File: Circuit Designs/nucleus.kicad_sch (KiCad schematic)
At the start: 73 parts

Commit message: deleted previous version files
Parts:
- removed R? (x2): 22R, CoF_Resistor:R-0402, symbol CoE_Resistor:22R
- C34, C35, C36, C37, C38, C39, C40, C41, C42, C43, C44, C45, C46, C47, C48, C49, C50, C51, C52, C53, C54, C55: renamed from C?; footprint Capacitor_SMD:C_0402_1005Metric -> CoF_Capacitor:C-0402
- gave numbers to parts that had none: 49
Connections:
- net USBD+: now also U2.45 (PA12)
- net USBD-: now also U2.44 (PA11)

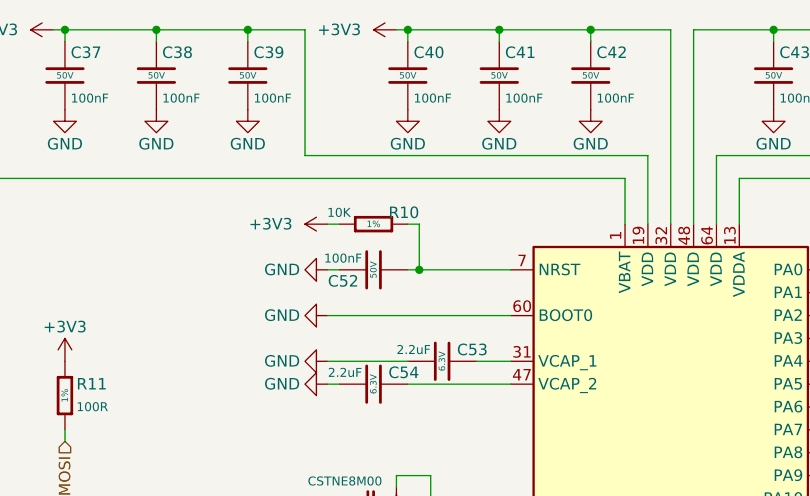
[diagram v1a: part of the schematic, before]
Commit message: changed the LED packages, edited field reference positions
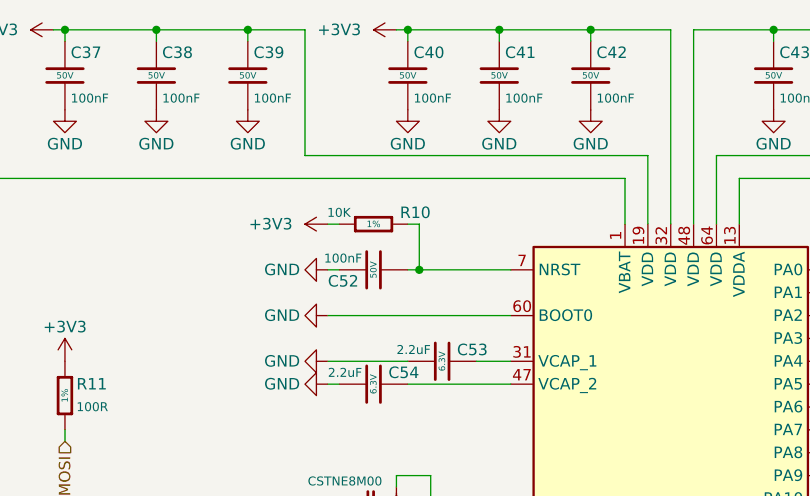
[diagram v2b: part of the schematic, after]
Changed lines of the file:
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@@
   (symbol (lib_id "CoE_Resistor:10K") (at 118.11 38.1 90) (unit 1)
     (in_bom yes) (on_board yes)
-    (property "Reference" "R10" (id 0) (at 123.19 36.83 90)
+    (property "Reference" "R10" (id 0) (at 124.46 36.83 90)
       (effects (font (size 1.27 1.27)) (justify left))
     )
@@
       (effects (font (size 1.27 1.27)) (justify bottom) hide)
     )
-    (property "Datasheet" "https://datasheet.lcsc.com/lcsc/1810231112_Hubei-KENTO-Elec-KT-0603R_C2286.pdf" (id 3) (at 233.172 147.574 0)
+    (property "Datasheet" "https://datasheet.lcsc.com/lcsc/1810231112_Hubei-KENTO-Elec-KT-0603R_C2286.pdf" (id 3) (at 219.71 162.56 0)
       (effects (font (size 1.27 1.27)) hide)
     )
@@
       (effects (font (size 1.27 1.27)) (justify bottom) hide)
     )
-    (property "Datasheet" "https://datasheet.lcsc.com/lcsc/1810011020_BrtLed-Bright-LED-Elec-BL-HJC36A-AV-TRB_C138546.pdf" (id 3) (at 68.072 147.574 0)
+    (property "Datasheet" "https://datasheet.lcsc.com/lcsc/1810011020_BrtLed-Bright-LED-Elec-BL-HJC36A-AV-TRB_C138546.pdf" (id 3) (at 54.61 162.56 0)
       (effects (font (size 1.27 1.27)) hide)
     )
@@
       (effects (font (size 1.27 1.27)) (justify bottom) hide)
     )
-    (property "Datasheet" "https://datasheet.lcsc.com/lcsc/1810231112_Hubei-KENTO-Elec-KT-0603R_C2286.pdf" (id 3) (at 80.772 147.574 0)
+    (property "Datasheet" "https://datasheet.lcsc.com/lcsc/1810231112_Hubei-KENTO-Elec-KT-0603R_C2286.pdf" (id 3) (at 67.31 162.56 0)
       (effects (font (size 1.27 1.27)) hide)
     )
@@
       (effects (font (size 1.27 1.27)) (justify bottom) hide)
     )
-    (property "Datasheet" "https://datasheet.lcsc.com/lcsc/1810011020_BrtLed-Bright-LED-Elec-BL-HJC36A-AV-TRB_C138546.pdf" (id 3) (at 93.472 147.574 0)
+    (property "Datasheet" "https://datasheet.lcsc.com/lcsc/1810011020_BrtLed-Bright-LED-Elec-BL-HJC36A-AV-TRB_C138546.pdf" (id 3) (at 80.01 162.56 0)
       (effects (font (size 1.27 1.27)) hide)
     )
@@
       (effects (font (size 1.27 1.27)) (justify bottom) hide)
     )
-    (property "Datasheet" "https://datasheet.lcsc.com/lcsc/1810231112_Hubei-KENTO-Elec-KT-0603R_C2286.pdf" (id 3) (at 106.172 147.574 0)
+    (property "Datasheet" "https://datasheet.lcsc.com/lcsc/1810231112_Hubei-KENTO-Elec-KT-0603R_C2286.pdf" (id 3) (at 92.71 162.56 0)
       (effects (font (size 1.27 1.27)) hide)
     )
@@
       (effects (font (size 1.27 1.27)) (justify bottom) hide)
     )
-    (property "Datasheet" "https://datasheet.lcsc.com/lcsc/1810011020_BrtLed-Bright-LED-Elec-BL-HJC36A-AV-TRB_C138546.pdf" (id 3) (at 118.872 147.574 0)
+    (property "Datasheet" "https://datasheet.lcsc.com/lcsc/1810011020_BrtLed-Bright-LED-Elec-BL-HJC36A-AV-TRB_C138546.pdf" (id 3) (at 105.41 162.56 0)
       (effects (font (size 1.27 1.27)) hide)
     )
@@
       (effects (font (size 1.27 1.27)) (justify bottom) hide)
     )
-    (property "Datasheet" "https://datasheet.lcsc.com/lcsc/1810231112_Hubei-KENTO-Elec-KT-0603R_C2286.pdf" (id 3) (at 131.572 147.574 0)
+    (property "Datasheet" "https://datasheet.lcsc.com/lcsc/1810231112_Hubei-KENTO-Elec-KT-0603R_C2286.pdf" (id 3) (at 118.11 162.56 0)
       (effects (font (size 1.27 1.27)) hide)
     )
@@
       (effects (font (size 1.27 1.27)) (justify bottom) hide)
     )
-    (property "Datasheet" "https://datasheet.lcsc.com/lcsc/1810011020_BrtLed-Bright-LED-Elec-BL-HJC36A-AV-TRB_C138546.pdf" (id 3) (at 144.272 147.574 0)
+    (property "Datasheet" "https://datasheet.lcsc.com/lcsc/1810011020_BrtLed-Bright-LED-Elec-BL-HJC36A-AV-TRB_C138546.pdf" (id 3) (at 130.81 162.56 0)
       (effects (font (size 1.27 1.27)) hide)
     )
@@
       (effects (font (size 1.27 1.27)) (justify bottom) hide)
     )
-    (property "Datasheet" "https://datasheet.lcsc.com/lcsc/1810231112_Hubei-KENTO-Elec-KT-0603R_C2286.pdf" (id 3) (at 156.972 147.574 0)
+    (property "Datasheet" "https://datasheet.lcsc.com/lcsc/1810231112_Hubei-KENTO-Elec-KT-0603R_C2286.pdf" (id 3) (at 143.51 162.56 0)
       (effects (font (size 1.27 1.27)) hide)
     )
@@
       (effects (font (size 1.27 1.27)) (justify bottom) hide)
     )
-    (property "Datasheet" "https://datasheet.lcsc.com/lcsc/1810011020_BrtLed-Bright-LED-Elec-BL-HJC36A-AV-TRB_C138546.pdf" (id 3) (at 169.672 147.574 0)
+    (property "Datasheet" "https://datasheet.lcsc.com/lcsc/1810011020_BrtLed-Bright-LED-Elec-BL-HJC36A-AV-TRB_C138546.pdf" (id 3) (at 156.21 162.56 0)
       (effects (font (size 1.27 1.27)) hide)
     )
@@
       (effects (font (size 1.27 1.27)) (justify bottom) hide)
     )
-    (property "Datasheet" "https://datasheet.lcsc.com/lcsc/1810231112_Hubei-KENTO-Elec-KT-0603R_C2286.pdf" (id 3) (at 182.372 147.574 0)
+    (property "Datasheet" "https://datasheet.lcsc.com/lcsc/1810231112_Hubei-KENTO-Elec-KT-0603R_C2286.pdf" (id 3) (at 168.91 162.56 0)
       (effects (font (size 1.27 1.27)) hide)
     )
@@
       (effects (font (size 1.27 1.27)) (justify bottom) hide)
     )
-    (property "Datasheet" "https://datasheet.lcsc.com/lcsc/1810011020_BrtLed-Bright-LED-Elec-BL-HJC36A-AV-TRB_C138546.pdf" (id 3) (at 195.072 147.574 0)
+    (property "Datasheet" "https://datasheet.lcsc.com/lcsc/1810011020_BrtLed-Bright-LED-Elec-BL-HJC36A-AV-TRB_C138546.pdf" (id 3) (at 181.61 162.56 0)
       (effects (font (size 1.27 1.27)) hide)
     )
@@
       (effects (font (size 1.27 1.27)) (justify bottom) hide)
     )
-    (property "Datasheet" "https://datasheet.lcsc.com/lcsc/1810231112_Hubei-KENTO-Elec-KT-0603R_C2286.pdf" (id 3) (at 207.772 147.574 0)
+    (property "Datasheet" "https://datasheet.lcsc.com/lcsc/1810231112_Hubei-KENTO-Elec-KT-0603R_C2286.pdf" (id 3) (at 194.31 162.56 0)
       (effects (font (size 1.27 1.27)) hide)
     )
@@
       (effects (font (size 1.27 1.27)) (justify bottom) hide)
     )
-    (property "Datasheet" "https://datasheet.lcsc.com/lcsc/1810011020_BrtLed-Bright-LED-Elec-BL-HJC36A-AV-TRB_C138546.pdf" (id 3) (at 220.472 147.574 0)
+    (property "Datasheet" "https://datasheet.lcsc.com/lcsc/1810011020_BrtLed-Bright-LED-Elec-BL-HJC36A-AV-TRB_C138546.pdf" (id 3) (at 207.01 162.56 0)
       (effects (font (size 1.27 1.27)) hide)
     )
@@
       (effects (font (size 1.27 1.27)) (justify bottom) hide)
     )
-    (property "Datasheet" "https://datasheet.lcsc.com/lcsc/1810011020_BrtLed-Bright-LED-Elec-BL-HJC36A-AV-TRB_C138546.pdf" (id 3) (at 245.872 147.574 0)
+    (property "Datasheet" "https://datasheet.lcsc.com/lcsc/1810011020_BrtLed-Bright-LED-Elec-BL-HJC36A-AV-TRB_C138546.pdf" (id 3) (at 232.41 162.56 0)
       (effects (font (size 1.27 1.27)) hide)
     )
@@
       (effects (font (size 1.27 1.27)) (justify bottom) hide)
     )
-    (property "Datasheet" "https://datasheet.lcsc.com/lcsc/1810231112_Hubei-KENTO-Elec-KT-0603R_C2286.pdf" (id 3) (at 258.572 147.574 0)
+    (property "Datasheet" "https://datasheet.lcsc.com/lcsc/1810231112_Hubei-KENTO-Elec-KT-0603R_C2286.pdf" (id 3) (at 245.11 162.56 0)
       (effects (font (size 1.27 1.27)) hide)
     )
@@
       (effects (font (size 1.27 1.27)) (justify bottom) hide)
     )
-    (property "Datasheet" "https://datasheet.lcsc.com/lcsc/1810011020_BrtLed-Bright-LED-Elec-BL-HJC36A-AV-TRB_C138546.pdf" (id 3) (at 271.272 147.574 0)
-      (effects (font (size 1.27 1.27)) hide)
-    )
+    (property "Datasheet" "https://datasheet.lcsc.com/lcsc/1810011020_BrtLed-Bright-LED-Elec-BL-HJC36A-AV-TRB_C138546.pdf" (id 3) (at 257.81 162.56 0)
+      (effects (font (size 1.27 1.27)) hide)
+    )

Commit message: edited the motor driver's and the current amplifier's packages
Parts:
- D1, D10, D11, D12, D13, D14, D15, D16, D17, D2, D3, D4, D5, D6, D7, D8, D9: footprint LED_SMD:LED_0603_1608Metric -> CoF_Diode:LED-0603
- Q1, Q2: footprint Package_TO_SOT_SMD:TSOT-23 -> CoF_SmallOutline:SOT-23
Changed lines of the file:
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@@
       (effects (font (size 0.9906 0.9906)) (justify left))
     )
-    (property "Footprint" "Package_TO_SOT_SMD:TSOT-23" (id 2) (at 99.06 154.94 0)
+    (property "Footprint" "CoF_SmallOutline:SOT-23" (id 2) (at 99.06 154.94 0)
       (effects (font (size 1.27 1.27)) (justify bottom) hide)
     )
@@
       (effects (font (size 0.9906 0.9906)) (justify left))
     )
-    (property "Footprint" "Package_TO_SOT_SMD:TSOT-23" (id 2) (at 74.93 154.94 0)
+    (property "Footprint" "CoF_SmallOutline:SOT-23" (id 2) (at 74.93 154.94 0)
       (effects (font (size 1.27 1.27)) (justify bottom) hide)
     )
@@
       (effects (font (size 0.9906 0.9906)) (justify left))
     )
-    (property "Footprint" "LED_SMD:LED_0603_1608Metric" (id 2) (at 219.71 135.89 0)
+    (property "Footprint" "CoF_Diode:LED-0603" (id 2) (at 219.71 135.89 0)
       (effects (font (size 1.27 1.27)) (justify bottom) hide)
     )
@@
       (effects (font (size 0.9906 0.9906)) (justify left))
     )
-    (property "Footprint" "LED_SMD:LED_0603_1608Metric" (id 2) (at 54.61 135.89 0)
+    (property "Footprint" "CoF_Diode:LED-0603" (id 2) (at 54.61 135.89 0)
       (effects (font (size 1.27 1.27)) (justify bottom) hide)
     )
@@
       (effects (font (size 0.9906 0.9906)) (justify left))
     )
-    (property "Footprint" "LED_SMD:LED_0603_1608Metric" (id 2) (at 67.31 135.89 0)
+    (property "Footprint" "CoF_Diode:LED-0603" (id 2) (at 67.31 135.89 0)
       (effects (font (size 1.27 1.27)) (justify bottom) hide)
     )
@@
       (effects (font (size 0.9906 0.9906)) (justify left))
     )
-    (property "Footprint" "LED_SMD:LED_0603_1608Metric" (id 2) (at 80.01 135.89 0)
+    (property "Footprint" "CoF_Diode:LED-0603" (id 2) (at 80.01 135.89 0)
       (effects (font (size 1.27 1.27)) (justify bottom) hide)
     )
@@
       (effects (font (size 0.9906 0.9906)) (justify left))
     )
-    (property "Footprint" "LED_SMD:LED_0603_1608Metric" (id 2) (at 92.71 135.89 0)
+    (property "Footprint" "CoF_Diode:LED-0603" (id 2) (at 92.71 135.89 0)
       (effects (font (size 1.27 1.27)) (justify bottom) hide)
     )
@@
       (effects (font (size 0.9906 0.9906)) (justify left))
     )
-    (property "Footprint" "LED_SMD:LED_0603_1608Metric" (id 2) (at 105.41 135.89 0)
+    (property "Footprint" "CoF_Diode:LED-0603" (id 2) (at 105.41 135.89 0)
       (effects (font (size 1.27 1.27)) (justify bottom) hide)
     )
@@
       (effects (font (size 0.9906 0.9906)) (justify left))
     )
-    (property "Footprint" "LED_SMD:LED_0603_1608Metric" (id 2) (at 118.11 135.89 0)
+    (property "Footprint" "CoF_Diode:LED-0603" (id 2) (at 118.11 135.89 0)
       (effects (font (size 1.27 1.27)) (justify bottom) hide)
     )
@@
       (effects (font (size 0.9906 0.9906)) (justify left))
     )
-    (property "Footprint" "LED_SMD:LED_0603_1608Metric" (id 2) (at 130.81 135.89 0)
+    (property "Footprint" "CoF_Diode:LED-0603" (id 2) (at 130.81 135.89 0)
       (effects (font (size 1.27 1.27)) (justify bottom) hide)
     )
@@
       (effects (font (size 0.9906 0.9906)) (justify left))
     )
-    (property "Footprint" "LED_SMD:LED_0603_1608Metric" (id 2) (at 143.51 135.89 0)
+    (property "Footprint" "CoF_Diode:LED-0603" (id 2) (at 143.51 135.89 0)
       (effects (font (size 1.27 1.27)) (justify bottom) hide)
     )
@@
       (effects (font (size 0.9906 0.9906)) (justify left))
     )
-    (property "Footprint" "LED_SMD:LED_0603_1608Metric" (id 2) (at 156.21 135.89 0)
+    (property "Footprint" "CoF_Diode:LED-0603" (id 2) (at 156.21 135.89 0)
       (effects (font (size 1.27 1.27)) (justify bottom) hide)
     )
@@
       (effects (font (size 0.9906 0.9906)) (justify left))
     )
-    (property "Footprint" "LED_SMD:LED_0603_1608Metric" (id 2) (at 168.91 135.89 0)
+    (property "Footprint" "CoF_Diode:LED-0603" (id 2) (at 168.91 135.89 0)
       (effects (font (size 1.27 1.27)) (justify bottom) hide)
     )
@@
       (effects (font (size 0.9906 0.9906)) (justify left))
     )
-    (property "Footprint" "LED_SMD:LED_0603_1608Metric" (id 2) (at 181.61 135.89 0)
+    (property "Footprint" "CoF_Diode:LED-0603" (id 2) (at 181.61 135.89 0)
       (effects (font (size 1.27 1.27)) (justify bottom) hide)
     )
@@
       (effects (font (size 0.9906 0.9906)) (justify left))
     )
-    (property "Footprint" "LED_SMD:LED_0603_1608Metric" (id 2) (at 194.31 135.89 0)
+    (property "Footprint" "CoF_Diode:LED-0603" (id 2) (at 194.31 135.89 0)
       (effects (font (size 1.27 1.27)) (justify bottom) hide)
     )
@@
       (effects (font (size 0.9906 0.9906)) (justify left))
     )
-    (property "Footprint" "LED_SMD:LED_0603_1608Metric" (id 2) (at 207.01 135.89 0)
+    (property "Footprint" "CoF_Diode:LED-0603" (id 2) (at 207.01 135.89 0)
       (effects (font (size 1.27 1.27)) (justify bottom) hide)
     )
@@
       (effects (font (size 0.9906 0.9906)) (justify left))
     )
-    (property "Footprint" "LED_SMD:LED_0603_1608Metric" (id 2) (at 232.41 135.89 0)
+    (property "Footprint" "CoF_Diode:LED-0603" (id 2) (at 232.41 135.89 0)
       (effects (font (size 1.27 1.27)) (justify bottom) hide)
     )
@@
       (effects (font (size 0.9906 0.9906)) (justify left))
     )
-    (property "Footprint" "LED_SMD:LED_0603_1608Metric" (id 2) (at 245.11 135.89 0)
+    (property "Footprint" "CoF_Diode:LED-0603" (id 2) (at 245.11 135.89 0)
       (effects (font (size 1.27 1.27)) (justify bottom) hide)
     )
@@
       (effects (font (size 0.9906 0.9906)) (justify left))
     )
-    (property "Footprint" "LED_SMD:LED_0603_1608Metric" (id 2) (at 257.81 135.89 0)
-      (effects (font (size 1.27 1.27)) (justify bottom) hide)
-    )
+    (property "Footprint" "CoF_Diode:LED-0603" (id 2) (at 257.81 135.89 0)
+      (effects (font (size 1.27 1.27)) (justify bottom) hide)
+    )

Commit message: done all the packages and migrations. Now, time to start to route the module
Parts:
- J5: footprint (none) -> CoF_Connector:SoicBite
- U2: footprint Package_QFP:LQFP-64_10x10mm_P0.5mm -> CoF_QuadFlat:LQFP-64
- Y1: footprint (none) -> CoF_Crystal:CSTNE

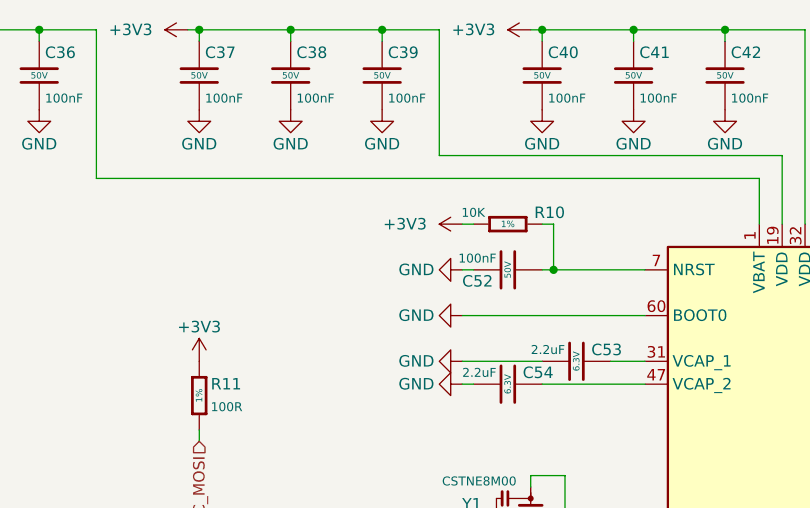
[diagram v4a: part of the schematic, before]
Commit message: done the connection between the MCU and the motor driver
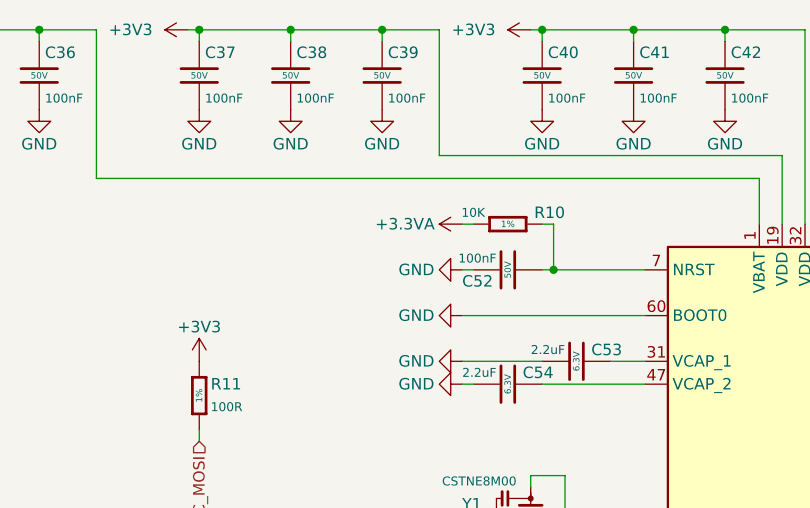
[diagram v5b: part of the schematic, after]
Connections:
- net +3.3VA: now also R10.1
- net +3V3: no longer R10.1
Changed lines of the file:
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@@
-    (pin "1")
-  )
-  (symbol (lib_id "power:+3V3") (at 113.03 38.1 90) (unit 1)
-    (in_bom yes) (on_board yes)
-    (property "Reference" "#PWR060" (id 0) (at 116.84 38.1 0)
-      (effects (font (size 1.27 1.27)) hide)
-    )
-    (property "Value" "+3V3" (id 1) (at 106.68 38.1 90))
-    (property "Footprint" "" (id 2) (at 113.03 38.1 0)
-      (effects (font (size 1.27 1.27)) hide)
-    )
-    (property "Datasheet" "" (id 3) (at 113.03 38.1 0)
-      (effects (font (size 1.27 1.27)) hide)
-    )
     (pin "1")
   )
@@
     (pin "2")
   )
+  (symbol (lib_id "power:+3.3VA") (at 113.03 38.1 90) (unit 1)
+    (in_bom yes) (on_board yes)
+    (property "Reference" "#PWR?" (id 0) (at 116.84 38.1 0)
+      (effects (font (size 1.27 1.27)) hide)
+    )
+    (property "Value" "+3.3VA" (id 1) (at 106.68 38.1 90))
+    (property "Footprint" "" (id 2) (at 113.03 38.1 0)
+      (effects (font (size 1.27 1.27)) hide)
+    )
+    (property "Datasheet" "" (id 3) (at 113.03 38.1 0)
+      (effects (font (size 1.27 1.27)) hide)
+    )
+    (pin "1")
+  )
 )

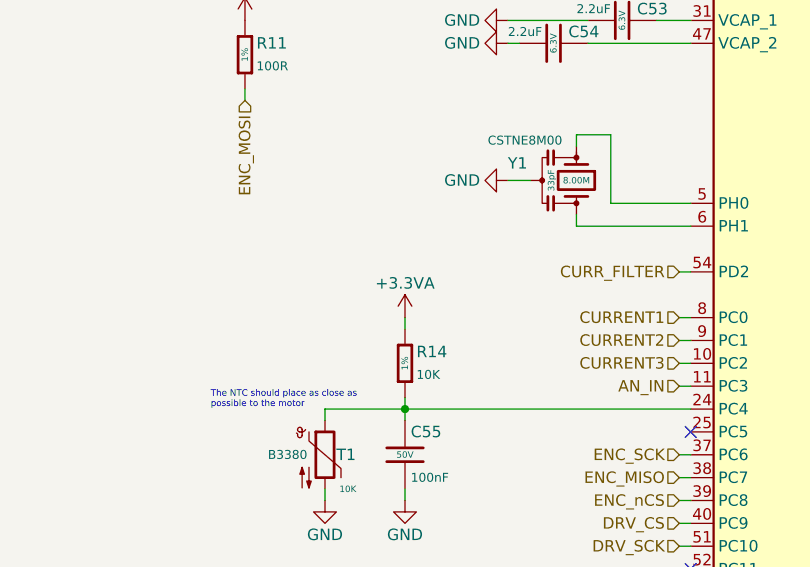
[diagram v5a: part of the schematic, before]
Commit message: done all the tracing between the driver and the mosfets
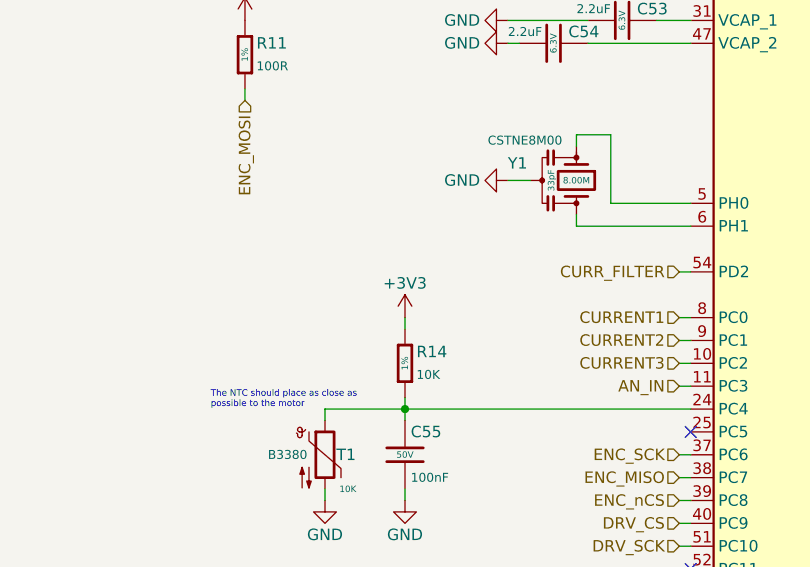
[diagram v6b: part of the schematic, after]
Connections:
- net +3.3VA: no longer R14.1
- net +3V3: now also R14.1
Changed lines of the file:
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@@
-    (pin "1")
-  )
-  (symbol (lib_id "power:+3.3VA") (at 101.6 86.36 0) (unit 1)
-    (in_bom yes) (on_board yes)
-    (property "Reference" "#PWR069" (id 0) (at 101.6 90.17 0)
-      (effects (font (size 1.27 1.27)) hide)
-    )
-    (property "Value" "+3.3VA" (id 1) (at 101.6 82.55 0))
-    (property "Footprint" "" (id 2) (at 101.6 86.36 0)
-      (effects (font (size 1.27 1.27)) hide)
-    )
-    (property "Datasheet" "" (id 3) (at 101.6 86.36 0)
-      (effects (font (size 1.27 1.27)) hide)
-    )
     (pin "1")
   )
@@
       (effects (font (size 1.27 1.27)) hide)
     )
+    (pin "1")
+  )
+  (symbol (lib_id "power:+3V3") (at 101.6 86.36 0) (unit 1)
+    (in_bom yes) (on_board yes)
+    (property "Reference" "#PWR?" (id 0) (at 101.6 90.17 0)
+      (effects (font (size 1.27 1.27)) hide)
+    )
+    (property "Value" "+3V3" (id 1) (at 101.6 82.55 0))
+    (property "Footprint" "" (id 2) (at 101.6 86.36 0)
+      (effects (font (size 1.27 1.27)) hide)
+    )
+    (property "Datasheet" "" (id 3) (at 101.6 86.36 0)
+      (effects (font (size 1.27 1.27)) hide)
+    )
